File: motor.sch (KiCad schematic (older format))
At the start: 44 parts, among them J16 70543-0003, Q10 PMPB20EN, Q3 PMPB20EN, Q4 PMPB20EN, Q5 PMPB20EN, Q6 PMPB20EN, Q7 PMPB20EN, Q8 PMPB20EN, Q9 PMPB20EN, U6 TMC2160-TA

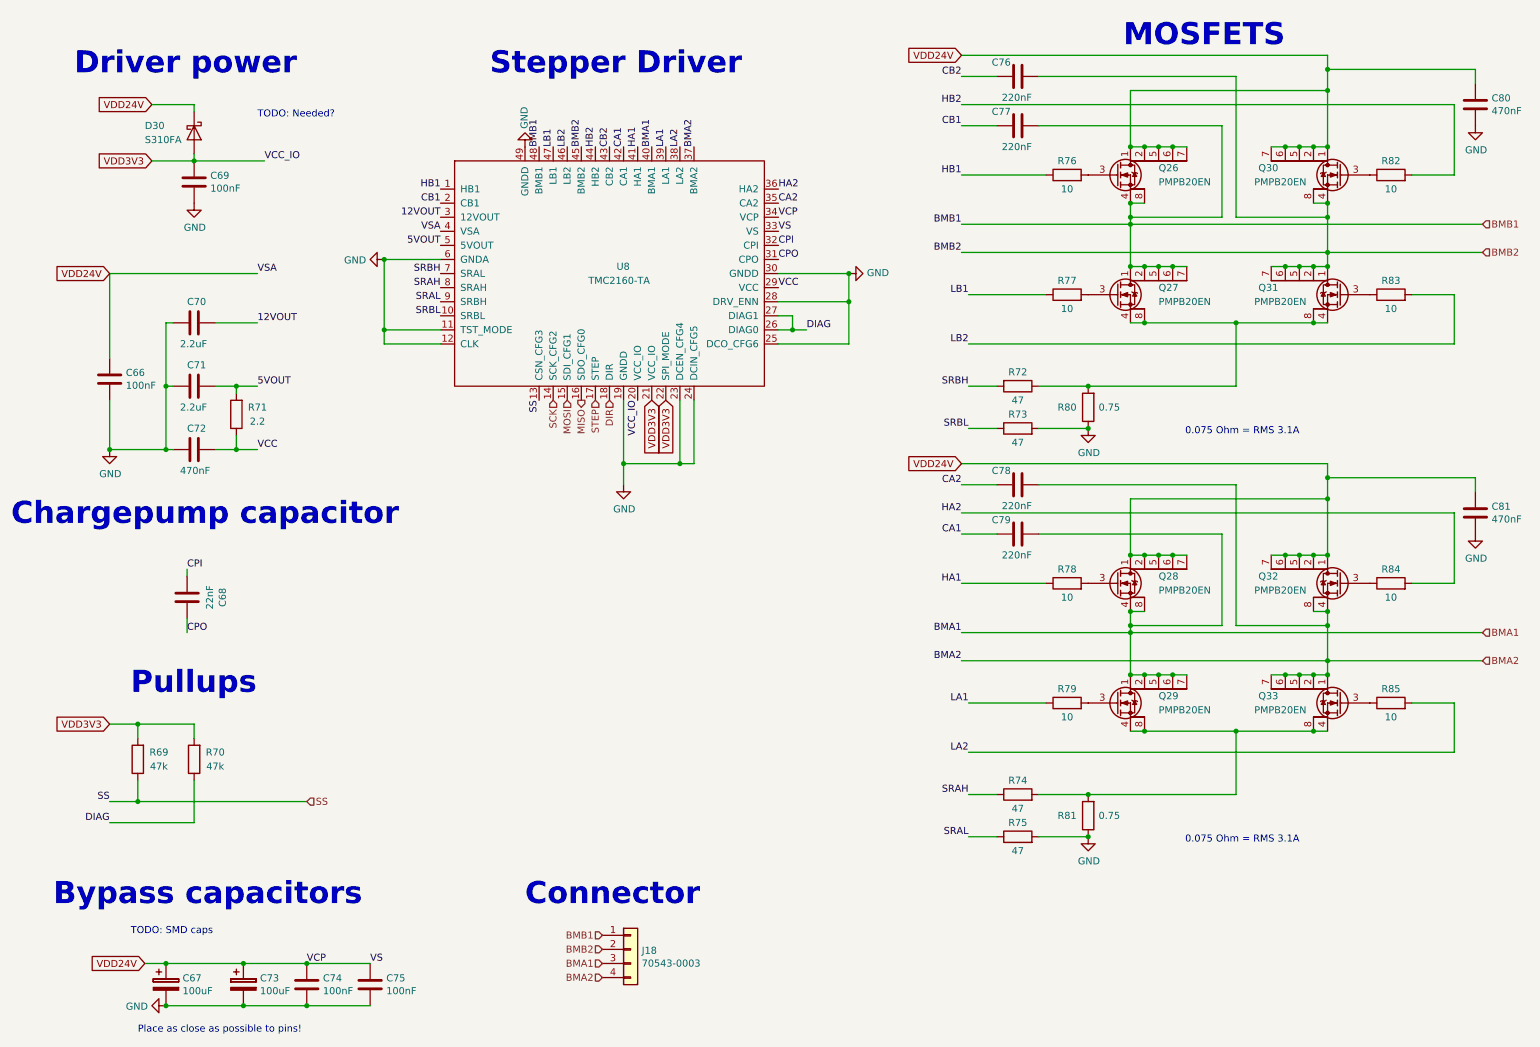
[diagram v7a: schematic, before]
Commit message: Various changes
* Add Status LED
* Switched small diodes to more general available BAT54 in SOD123
* Fixed various DRC errors
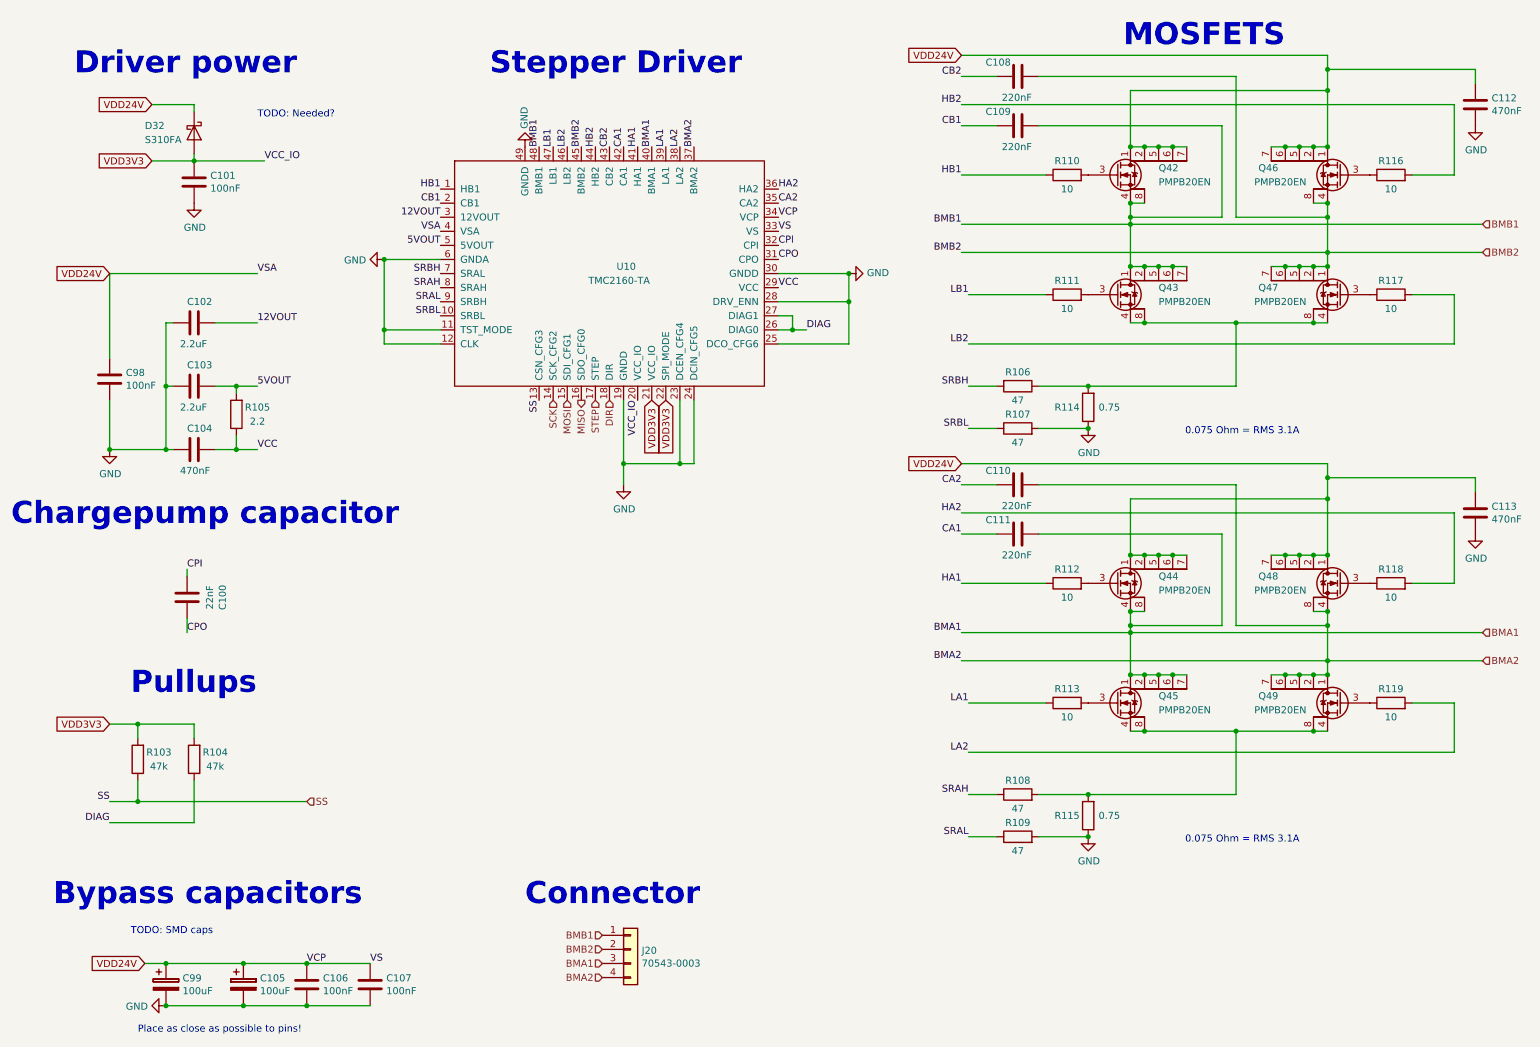
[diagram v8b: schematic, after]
